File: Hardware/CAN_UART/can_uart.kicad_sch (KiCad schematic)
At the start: 0 parts

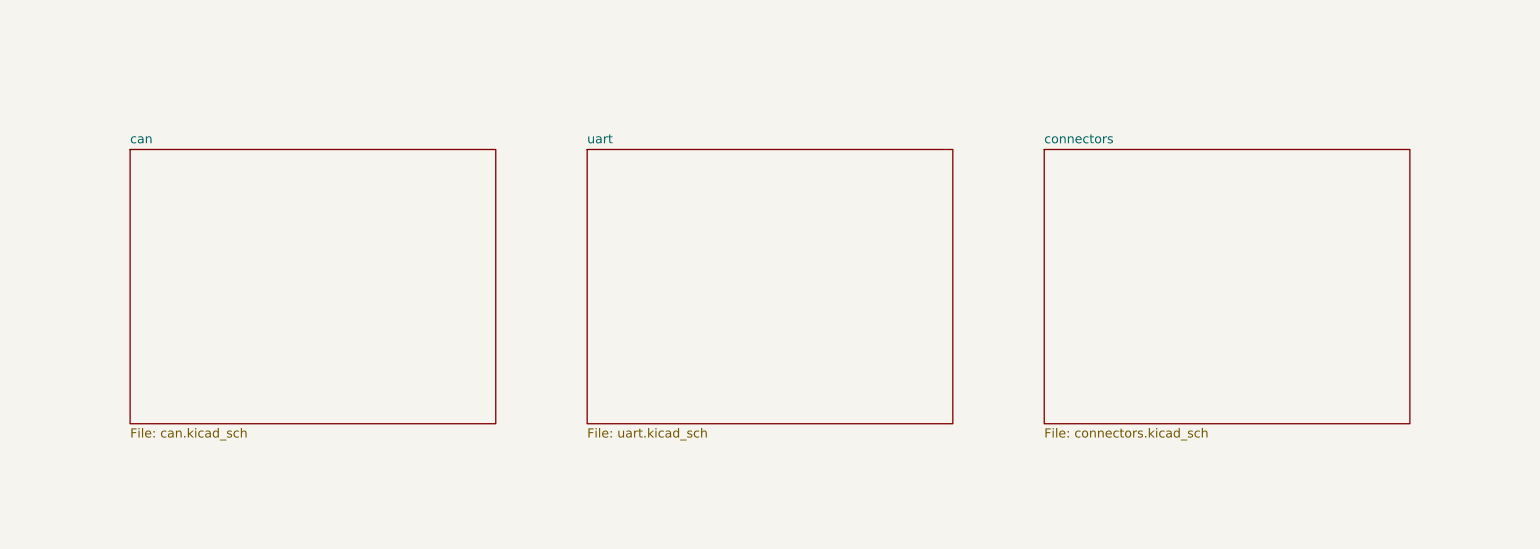
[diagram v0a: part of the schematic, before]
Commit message: analog & can finished
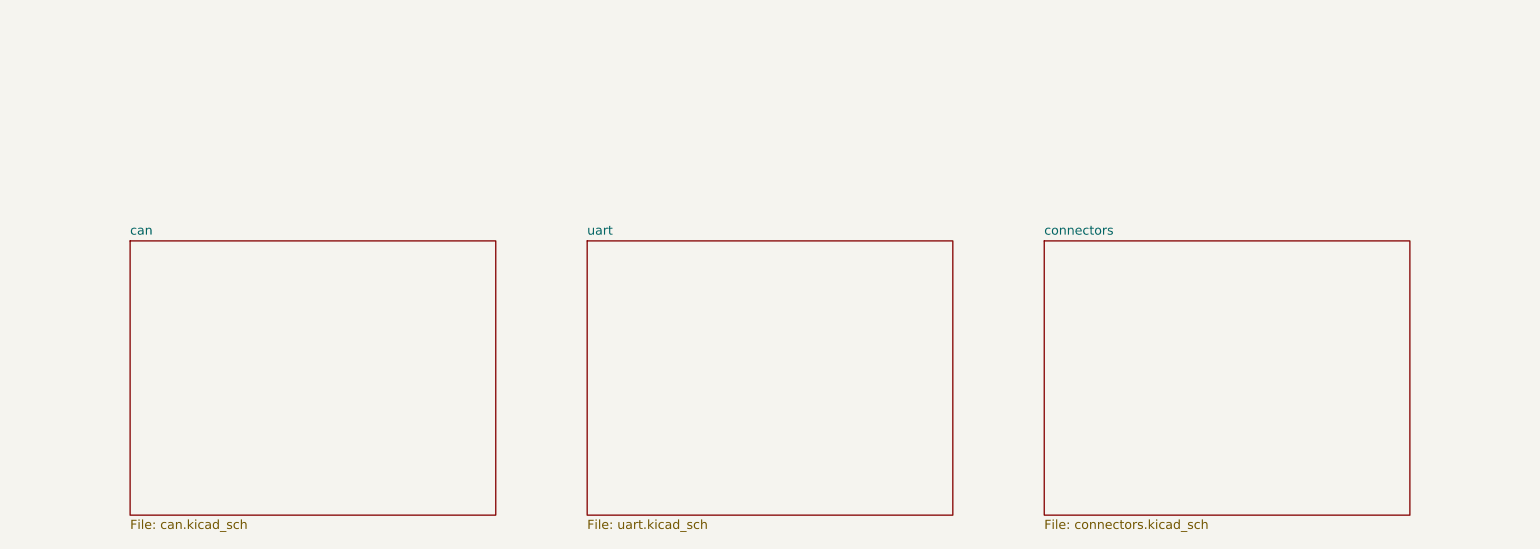
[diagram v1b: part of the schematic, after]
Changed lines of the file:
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@@
 	)
 	(sheet
-		(at 127 76.2)
+		(at 127 88.9)
 		(size 50.8 38.1)
 		(exclude_from_sim no)
@@
 		)
 		(property "Sheetname" "uart"
-			(at 127 75.4884 0)
+			(at 127 88.1884 0)
 			(effects
 				(font
@@
 		)
 		(property "Sheetfile" "uart.kicad_sch"
-			(at 127 114.8846 0)
+			(at 127 127.5846 0)
 			(effects
 				(font
@@
 	)
 	(sheet
-		(at 63.5 76.2)
+		(at 63.5 88.9)
 		(size 50.8 38.1)
 		(exclude_from_sim no)
@@
 		)
 		(property "Sheetname" "can"
-			(at 63.5 75.4884 0)
+			(at 63.5 88.1884 0)
 			(effects
 				(font
@@
 		)
 		(property "Sheetfile" "can.kicad_sch"
-			(at 63.5 114.8846 0)
+			(at 63.5 127.5846 0)
 			(effects
 				(font
@@
 	)
 	(sheet
-		(at 190.5 76.2)
+		(at 190.5 88.9)
 		(size 50.8 38.1)
 		(exclude_from_sim no)
@@
 		)
 		(property "Sheetname" "connectors"
-			(at 190.5 75.4884 0)
+			(at 190.5 88.1884 0)
 			(effects
 				(font
@@
 		)
 		(property "Sheetfile" "connectors.kicad_sch"
-			(at 190.5 114.8846 0)
+			(at 190.5 127.5846 0)
 			(effects
 				(font
